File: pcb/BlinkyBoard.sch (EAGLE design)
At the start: 26 parts, among them Q1 16 MHz

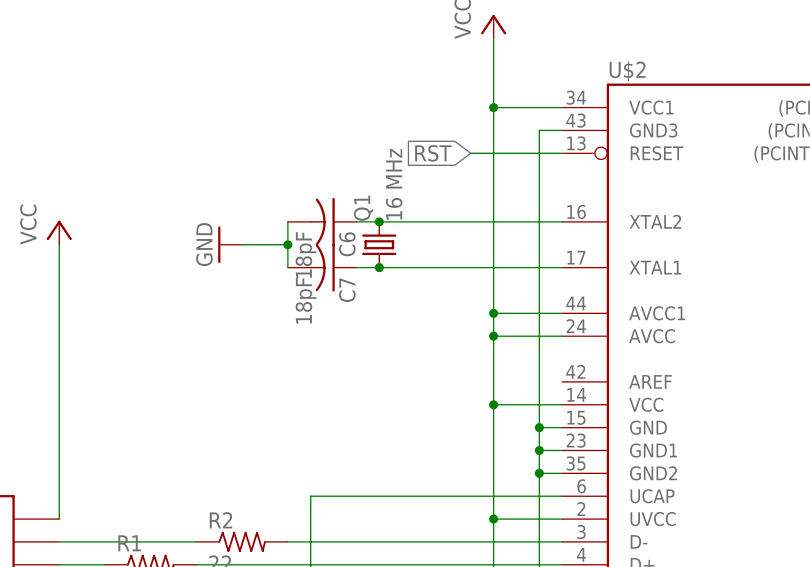
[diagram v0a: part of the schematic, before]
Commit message: Almost have D7 squeezed in, clean up silk
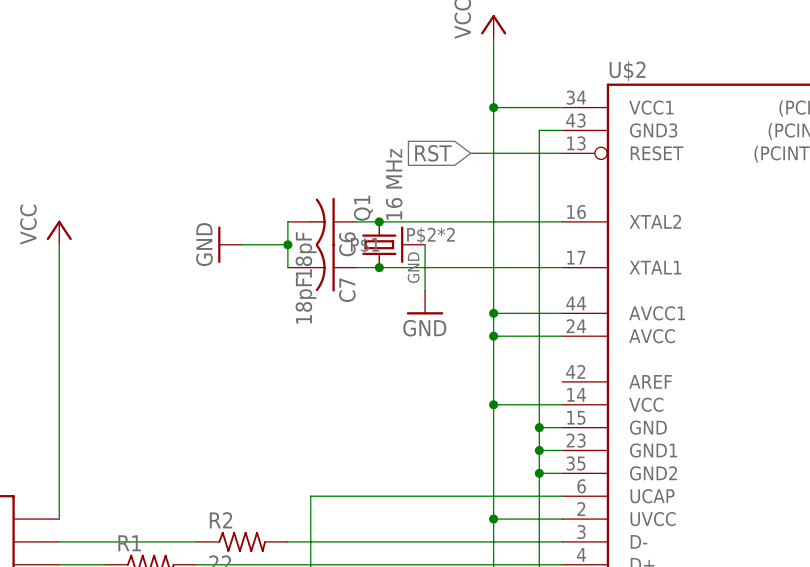
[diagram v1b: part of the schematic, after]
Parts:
- Q1: device blinkiverse:CRYSTAL2520 -> blinkiverse:CRYSTAL_4PAD2520
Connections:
- net GND: now also Q1.P$1
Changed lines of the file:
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@@
 <part name="P+7" library="supply1" deviceset="VCC" device=""/>
 <part name="S1" library="blinkyboard" deviceset="GLOWBOARD_KMR211G" device="" value="Normally open"/>
-<part name="Q1" library="blinkiverse" deviceset="CRYSTAL" device="2520" value="16 MHz"/>
+<part name="Q1" library="blinkiverse" deviceset="CRYSTAL_4PAD" device="2520" value="16 MHz"/>
 <part name="C4" library="blinkiverse" deviceset="C_US" device="" value="0.1uF"/>
 <part name="WS1" library="blinkiverse" deviceset="WS2811_CONNECTOR" device=""/>
@@
 <part name="U$13" library="blinkiverse" deviceset="TEST_PAD_SMT" device=""/>
 <part name="U$14" library="blinkiverse" deviceset="TEST_PAD_SMT" device=""/>
+<part name="GND9" library="supply1" deviceset="GND" device=""/>
 </parts>
 <sheets>
@@
 <instance part="U$13" gate="G$1" x="187.96" y="86.36"/>
 <instance part="U$14" gate="G$1" x="187.96" y="93.98"/>
+<instance part="GND9" gate="1" x="20.32" y="63.5"/>
 </instances>
 <busses>
@@
 <pinref part="U$13" gate="G$1" pin="P$1"/>
 </segment>
+<segment>
+<pinref part="Q1" gate="G$1" pin="P$1"/>
+<pinref part="GND9" gate="1" pin="GND"/>
+<wire x1="20.32" y1="71.12" x2="20.32" y2="66.04" width="0.1524" layer="91"/>
+</segment>
 </net>

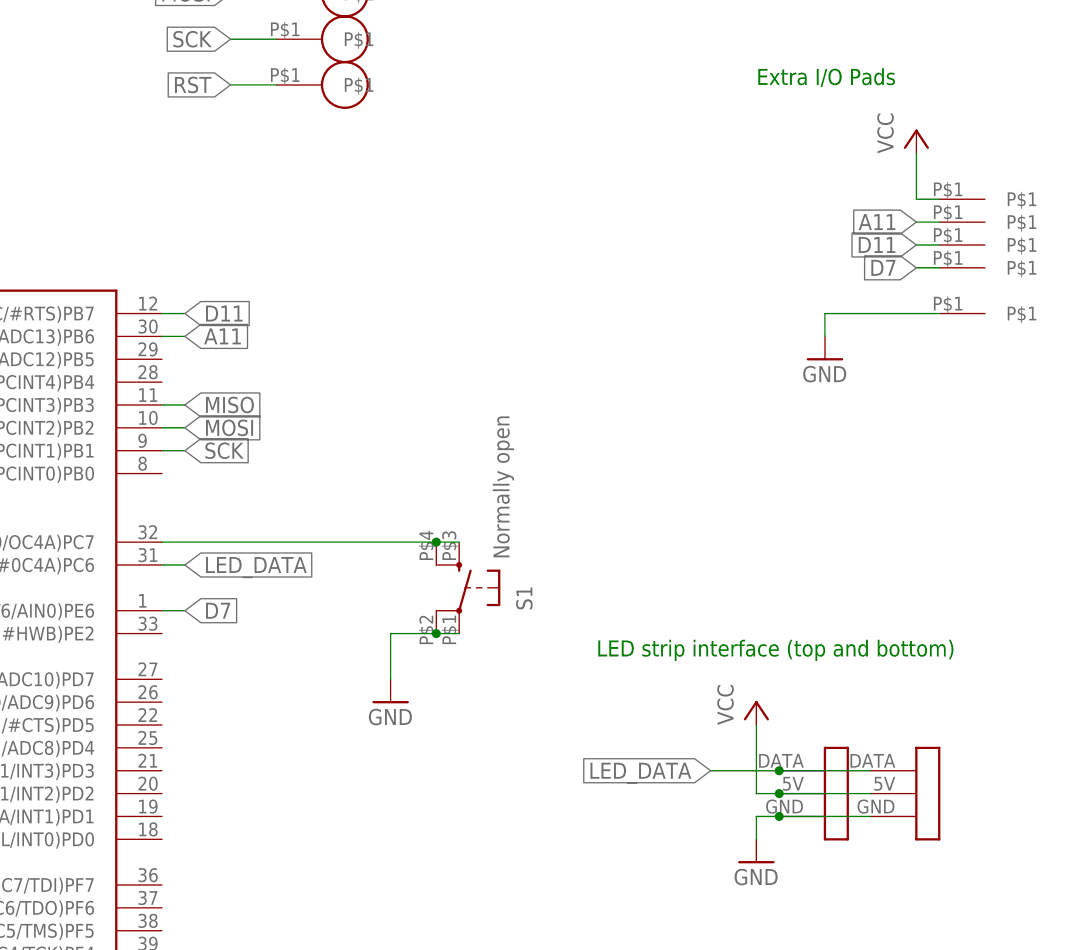
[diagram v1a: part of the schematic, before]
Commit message: RevD candidate- Move switch to D10 (for interrupt capability), then move analog input to A10 and LED_DATA to D13.
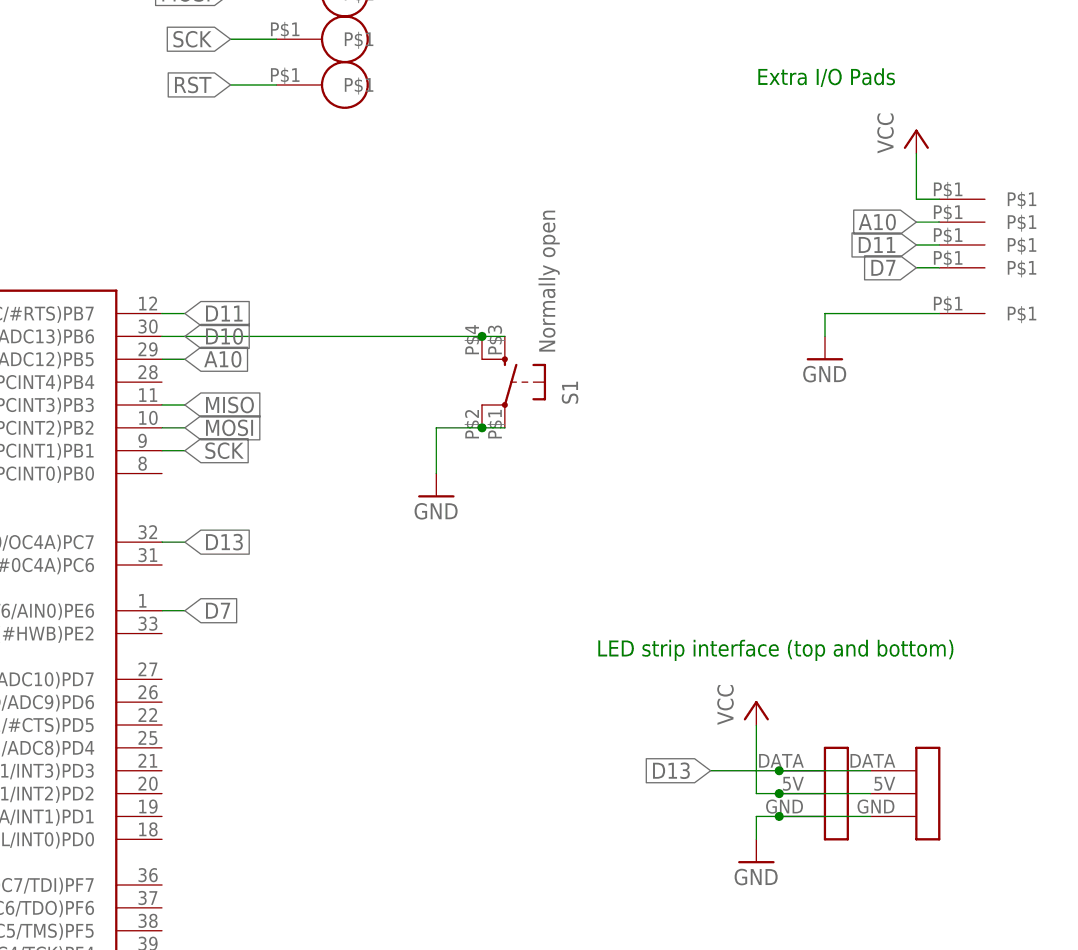
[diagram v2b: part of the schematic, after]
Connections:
- removed net A11: U$11.P$1, U$2.(PCINT6/OC1B/OC4B/ADC13)PB6
- removed net LED_DATA: U$2.(OC3A/#0C4A)PC6, WS1.DATA, WS3.DATA
- removed net N$10: S1.S, S1.S1, U$2.(ICP3/CLK0/OC4A)PC7
- new net A10: U$11.P$1, U$2.(PCINT5/OC1A/#OC4B/ADC12)PB5
- new net D10: S1.S, S1.S1, U$2.(PCINT6/OC1B/OC4B/ADC13)PB6
- new net D13: U$2.(ICP3/CLK0/OC4A)PC7, WS1.DATA, WS3.DATA
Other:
- moved on the sheet: S1
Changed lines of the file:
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@@
 <instance part="C3" gate="G$1" x="-30.48" y="121.92"/>
 <instance part="GND12" gate="1" x="-30.48" y="109.22" rot="MR0"/>
-<instance part="GND7" gate="1" x="121.92" y="43.18"/>
+<instance part="GND7" gate="1" x="127" y="66.04"/>
 <instance part="C6" gate="G$1" x="10.16" y="73.66" rot="R270"/>
 <instance part="C7" gate="G$1" x="10.16" y="68.58" rot="R270"/>
@@
 <instance part="P+6" gate="VCC" x="27.94" y="96.52"/>
 <instance part="P+7" gate="VCC" x="-30.48" y="132.08"/>
-<instance part="S1" gate="1" x="129.54" y="55.88" rot="MR0"/>
+<instance part="S1" gate="1" x="134.62" y="78.74" rot="MR0"/>
 <instance part="Q1" gate="G$1" x="15.24" y="71.12" rot="R90"/>
 <instance part="C4" gate="G$1" x="-20.32" y="121.92"/>
@@
 </segment>
 <segment>
-<wire x1="121.92" y1="45.72" x2="121.92" y2="50.8" width="0.1524" layer="91"/>
+<wire x1="127" y1="68.58" x2="127" y2="73.66" width="0.1524" layer="91"/>
 <pinref part="GND7" gate="1" pin="GND"/>
 <pinref part="S1" gate="1" pin="P"/>
 <pinref part="S1" gate="1" pin="P1"/>
-<wire x1="129.54" y1="50.8" x2="127" y2="50.8" width="0.1524" layer="91"/>
-<wire x1="127" y1="50.8" x2="121.92" y2="50.8" width="0.1524" layer="91"/>
-<junction x="127" y="50.8"/>
+<wire x1="134.62" y1="73.66" x2="132.08" y2="73.66" width="0.1524" layer="91"/>
+<wire x1="132.08" y1="73.66" x2="127" y2="73.66" width="0.1524" layer="91"/>
+<junction x="132.08" y="73.66"/>
 </segment>
 <segment>
@@
 </segment>
 </net>
-<net name="N$10" class="0">
-<segment>
-<pinref part="U$2" gate="G$1" pin="(ICP3/CLK0/OC4A)PC7"/>
+<net name="D10" class="0">
+<segment>
 <pinref part="S1" gate="1" pin="S1"/>
-<wire x1="96.52" y1="60.96" x2="127" y2="60.96" width="0.1524" layer="91"/>
 <pinref part="S1" gate="1" pin="S"/>
-<wire x1="129.54" y1="60.96" x2="127" y2="60.96" width="0.1524" layer="91"/>
-<junction x="127" y="60.96"/>
+<wire x1="134.62" y1="83.82" x2="132.08" y2="83.82" width="0.1524" layer="91"/>
+<pinref part="U$2" gate="G$1" pin="(PCINT6/OC1B/OC4B/ADC13)PB6"/>
+<wire x1="96.52" y1="83.82" x2="132.08" y2="83.82" width="0.1524" layer="91"/>
+<junction x="132.08" y="83.82"/>
+<label x="99.06" y="83.82" size="1.778" layer="95" xref="yes"/>
 </segment>
 </net>
@@
 </segment>
 </net>
-<net name="A11" class="0">
-<segment>
-<pinref part="U$2" gate="G$1" pin="(PCINT6/OC1B/OC4B/ADC13)PB6"/>
-<wire x1="96.52" y1="83.82" x2="99.06" y2="83.82" width="0.1524" layer="91"/>
-<label x="99.06" y="83.82" size="1.778" layer="95" xref="yes"/>
-</segment>
-<segment>
-<label x="180.34" y="96.52" size="1.778" layer="95" rot="R180" xref="yes"/>
-<wire x1="182.88" y1="96.52" x2="180.34" y2="96.52" width="0.1524" layer="91"/>
-<pinref part="U$11" gate="G$1" pin="P$1"/>
-</segment>
-</net>
-<net name="LED_DATA" class="0">
-<segment>
-<pinref part="U$2" gate="G$1" pin="(OC3A/#0C4A)PC6"/>
-<wire x1="96.52" y1="58.42" x2="99.06" y2="58.42" width="0.1524" layer="91"/>
-<label x="99.06" y="58.42" size="1.778" layer="95" xref="yes"/>
-</segment>
+<net name="D13" class="0">
 <segment>
 <pinref part="WS1" gate="G$1" pin="DATA"/>
@@
 <wire x1="175.26" y1="35.56" x2="165.1" y2="35.56" width="0.1524" layer="91"/>
 <junction x="165.1" y="35.56"/>
+</segment>
+<segment>
+<pinref part="U$2" gate="G$1" pin="(ICP3/CLK0/OC4A)PC7"/>
+<wire x1="96.52" y1="60.96" x2="99.06" y2="60.96" width="0.1524" layer="91"/>
+<label x="99.06" y="60.96" size="1.778" layer="95" xref="yes"/>
 </segment>
 </net>
@@
 </segment>
 </net>
+<net name="A10" class="0">
+<segment>
+<pinref part="U$2" gate="G$1" pin="(PCINT5/OC1A/#OC4B/ADC12)PB5"/>
+<wire x1="96.52" y1="81.28" x2="99.06" y2="81.28" width="0.1524" layer="91"/>
+<label x="99.06" y="81.28" size="1.778" layer="95" xref="yes"/>
+</segment>
+<segment>
+<label x="180.34" y="96.52" size="1.778" layer="95" rot="R180" xref="yes"/>
+<wire x1="182.88" y1="96.52" x2="180.34" y2="96.52" width="0.1524" layer="91"/>
+<pinref part="U$11" gate="G$1" pin="P$1"/>
+</segment>
+</net>

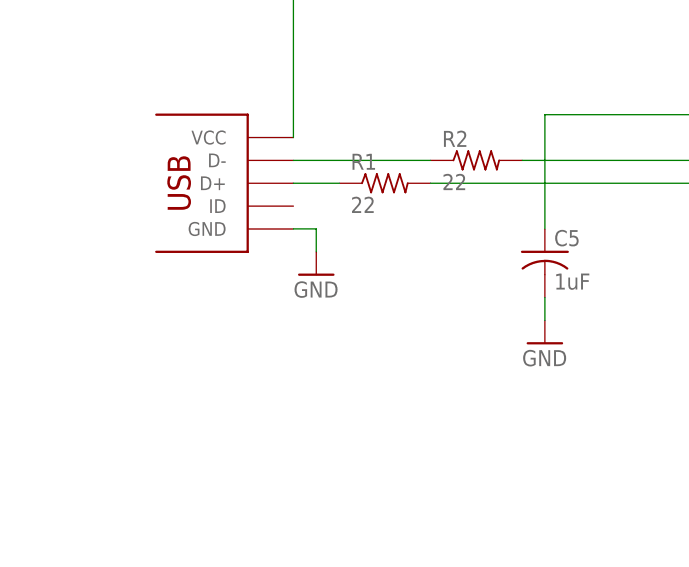
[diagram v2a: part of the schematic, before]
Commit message: Fix copper planes under usb connector
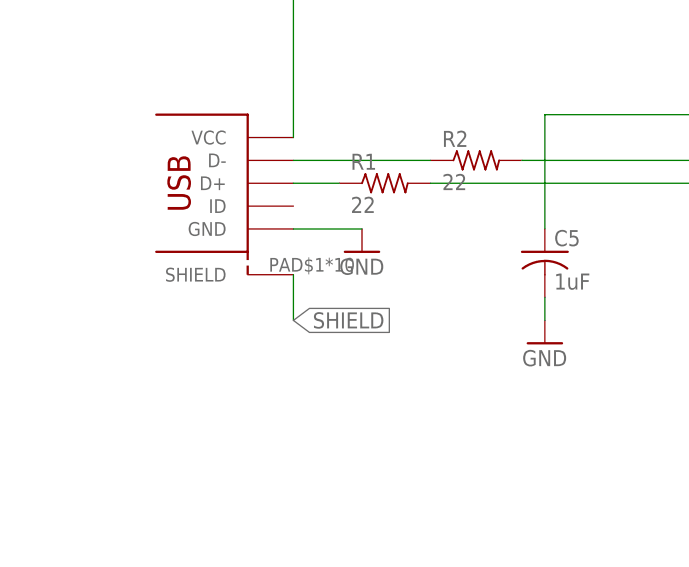
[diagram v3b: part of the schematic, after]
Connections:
- new net SHIELD: U$4.SHIELD
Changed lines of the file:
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@@
 <instance part="P+4" gate="VCC" x="-20.32" y="73.66"/>
 <instance part="U$4" gate="G$1" x="-27.94" y="35.56"/>
-<instance part="GND5" gate="1" x="-17.78" y="25.4"/>
+<instance part="GND5" gate="1" x="-12.7" y="27.94"/>
 <instance part="U$1" gate="G$1" x="114.3" y="127"/>
 <instance part="U$3" gate="G$1" x="114.3" y="121.92"/>
@@
 <segment>
 <pinref part="U$4" gate="G$1" pin="GND"/>
-<wire x1="-20.32" y1="30.48" x2="-17.78" y2="30.48" width="0.1524" layer="91"/>
+<wire x1="-20.32" y1="30.48" x2="-12.7" y2="30.48" width="0.1524" layer="91"/>
 <pinref part="GND5" gate="1" pin="GND"/>
-<wire x1="-17.78" y1="30.48" x2="-17.78" y2="27.94" width="0.1524" layer="91"/>
 </segment>
 <segment>
@@
 </segment>
 </net>
+<net name="SHIELD" class="0">
+<segment>
+<pinref part="U$4" gate="G$1" pin="SHIELD"/>
+<wire x1="-20.32" y1="25.4" x2="-20.32" y2="20.32" width="0.1524" layer="91"/>
+<label x="-20.32" y="20.32" size="1.778" layer="95" xref="yes"/>
+</segment>
+</net>

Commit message: Reorganize test designs, add test card, fix silk on main PCBA
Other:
- note added: "BlinkyTape LED controller RevD"
- note added: "http://blinkiverse.com"
- note removed: "BlinkyBoard LED controller RevB"
- note removed: "http://blinkyverse.com"
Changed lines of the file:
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@@
 <sheet>
 <plain>
-<text x="104.14" y="-30.48" size="2.54" layer="94">BlinkyBoard LED controller RevB</text>
-<text x="104.14" y="-35.56" size="2.54" layer="94">http://blinkyverse.com</text>
+<text x="104.14" y="-30.48" size="2.54" layer="94">BlinkyTape LED controller RevD</text>
+<text x="104.14" y="-35.56" size="2.54" layer="94">http://blinkiverse.com</text>
 <text x="177.8" y="-30.48" size="2.54" layer="94">CC 2.5 BY-SA</text>
 <text x="190.5" y="-53.34" size="2.54" layer="94">1</text>

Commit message: PCB design fix: add cream to all USB ground pads!
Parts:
- WS1, WS3: value WS2811_CONNECTOR -> WS2811_CONNECTORSTRIP; device blinkiverse:WS2811_CONNECTOR -> blinkiverse:WS2811_CONNECTORSTRIP
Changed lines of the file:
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@@
 <part name="Q1" library="blinkiverse" deviceset="CRYSTAL_4PAD" device="2520" value="16 MHz"/>
 <part name="C4" library="blinkiverse" deviceset="C_US" device="" value="0.1uF"/>
-<part name="WS1" library="blinkiverse" deviceset="WS2811_CONNECTOR" device=""/>
+<part name="WS1" library="blinkiverse" deviceset="WS2811_CONNECTOR" device="STRIP"/>
 <part name="P+3" library="supply1" deviceset="VCC" device=""/>
 <part name="GND4" library="supply1" deviceset="GND" device=""/>
@@
 <part name="GND1" library="supply1" deviceset="GND" device=""/>
 <part name="GND2" library="supply1" deviceset="GND" device=""/>
-<part name="WS3" library="blinkiverse" deviceset="WS2811_CONNECTOR" device=""/>
+<part name="WS3" library="blinkiverse" deviceset="WS2811_CONNECTOR" device="STRIP"/>
 <part name="P+5" library="supply1" deviceset="VCC" device=""/>
 <part name="U$10" library="blinkiverse" deviceset="TEST_PAD_SMT" device=""/>

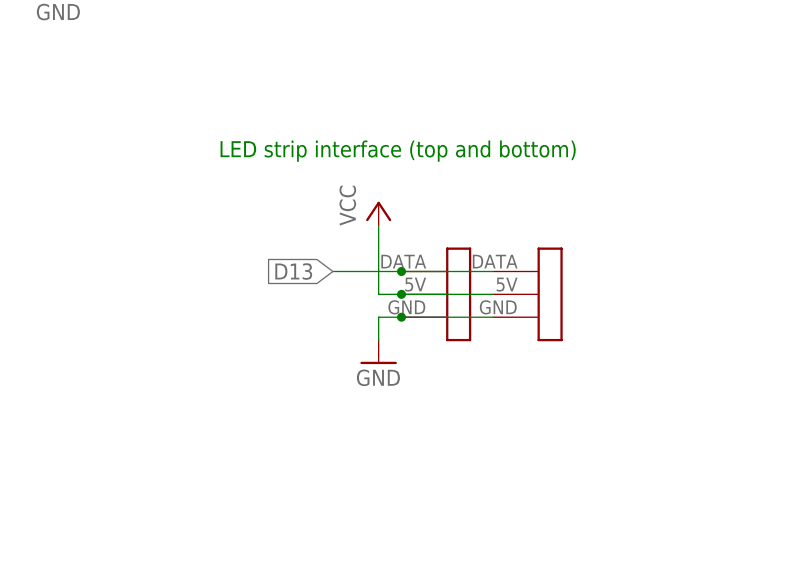
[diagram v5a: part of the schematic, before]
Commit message: RevF release: modify pads to support WS2811B
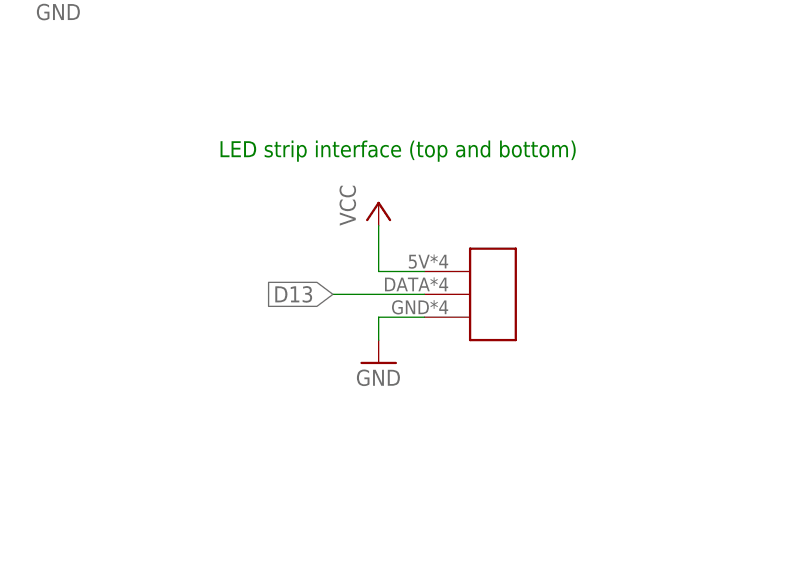
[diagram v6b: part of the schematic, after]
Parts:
- removed WS1, WS3: WS2811_CONNECTORSTRIP, blinkiverse:WS2811_CONNECTORSTRIP
- added U$9: WS2812B_CONNECTOR, blinkiverse:WS2812B_CONNECTOR
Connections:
- net D13: now also U$9.DATA; no longer WS1.DATA, WS3.DATA
- net GND: now also U$9.GND; no longer WS1.GND, WS3.GND
- net VCC: now also U$9.5V; no longer WS1.5V, WS3.5V
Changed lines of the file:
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@@
 <part name="Q1" library="blinkiverse" deviceset="CRYSTAL_4PAD" device="2520" value="16 MHz"/>
 <part name="C4" library="blinkiverse" deviceset="C_US" device="" value="0.1uF"/>
-<part name="WS1" library="blinkiverse" deviceset="WS2811_CONNECTOR" device="STRIP"/>
 <part name="P+3" library="supply1" deviceset="VCC" device=""/>
 <part name="GND4" library="supply1" deviceset="GND" device=""/>
@@
 <part name="GND1" library="supply1" deviceset="GND" device=""/>
 <part name="GND2" library="supply1" deviceset="GND" device=""/>
-<part name="WS3" library="blinkiverse" deviceset="WS2811_CONNECTOR" device="STRIP"/>
 <part name="P+5" library="supply1" deviceset="VCC" device=""/>
 <part name="U$10" library="blinkiverse" deviceset="TEST_PAD_SMT" device=""/>
@@
 <part name="U$14" library="blinkiverse" deviceset="TEST_PAD_SMT" device=""/>
 <part name="GND9" library="supply1" deviceset="GND" device=""/>
+<part name="U$9" library="blinkiverse" deviceset="WS2812B_CONNECTOR" device=""/>
 </parts>
 <sheets>
@@
 <instance part="Q1" gate="G$1" x="15.24" y="71.12" rot="R90"/>
 <instance part="C4" gate="G$1" x="-20.32" y="121.92"/>
-<instance part="WS1" gate="G$1" x="172.72" y="33.02"/>
 <instance part="P+3" gate="VCC" x="162.56" y="43.18"/>
 <instance part="GND4" gate="1" x="162.56" y="25.4"/>
@@
 <instance part="GND1" gate="1" x="101.6" y="132.08" rot="R270"/>
 <instance part="GND2" gate="1" x="170.18" y="81.28"/>
-<instance part="WS3" gate="G$1" x="182.88" y="33.02"/>
 <instance part="P+5" gate="VCC" x="180.34" y="106.68"/>
 <instance part="U$10" gate="G$1" x="187.96" y="91.44"/>
@@
 <instance part="U$14" gate="G$1" x="187.96" y="93.98"/>
 <instance part="GND9" gate="1" x="20.32" y="63.5"/>
+<instance part="U$9" gate="G$1" x="172.72" y="33.02"/>
 </instances>
 <busses>
@@
 </segment>
 <segment>
-<pinref part="WS1" gate="G$1" pin="GND"/>
-<wire x1="165.1" y1="30.48" x2="162.56" y2="30.48" width="0.1524" layer="91"/>
 <pinref part="GND4" gate="1" pin="GND"/>
 <wire x1="162.56" y1="30.48" x2="162.56" y2="27.94" width="0.1524" layer="91"/>
-<pinref part="WS3" gate="G$1" pin="GND"/>
-<wire x1="175.26" y1="30.48" x2="165.1" y2="30.48" width="0.1524" layer="91"/>
-<junction x="165.1" y="30.48"/>
+<pinref part="U$9" gate="G$1" pin="GND"/>
+<wire x1="162.56" y1="30.48" x2="167.64" y2="30.48" width="0.1524" layer="91"/>
 </segment>
 <segment>
@@
 <net name="D13" class="0">
 <segment>
-<pinref part="WS1" gate="G$1" pin="DATA"/>
-<wire x1="165.1" y1="35.56" x2="157.48" y2="35.56" width="0.1524" layer="91"/>
-<label x="157.48" y="35.56" size="1.778" layer="95" rot="R180" xref="yes"/>
-<pinref part="WS3" gate="G$1" pin="DATA"/>
-<wire x1="175.26" y1="35.56" x2="165.1" y2="35.56" width="0.1524" layer="91"/>
-<junction x="165.1" y="35.56"/>
-</segment>
-<segment>
 <pinref part="U$2" gate="G$1" pin="(ICP3/CLK0/OC4A)PC7"/>
 <wire x1="96.52" y1="60.96" x2="99.06" y2="60.96" width="0.1524" layer="91"/>
 <label x="99.06" y="60.96" size="1.778" layer="95" xref="yes"/>
+</segment>
+<segment>
+<wire x1="167.64" y1="33.02" x2="157.48" y2="33.02" width="0.1524" layer="91"/>
+<label x="157.48" y="33.02" size="1.778" layer="95" rot="R180" xref="yes"/>
+<pinref part="U$9" gate="G$1" pin="DATA"/>
 </segment>
 </net>
@@
 </segment>
 <segment>
-<pinref part="WS1" gate="G$1" pin="5V"/>
-<wire x1="165.1" y1="33.02" x2="162.56" y2="33.02" width="0.1524" layer="91"/>
 <pinref part="P+3" gate="VCC" pin="VCC"/>
-<wire x1="162.56" y1="33.02" x2="162.56" y2="40.64" width="0.1524" layer="91"/>
-<pinref part="WS3" gate="G$1" pin="5V"/>
-<wire x1="165.1" y1="33.02" x2="175.26" y2="33.02" width="0.1524" layer="91"/>
-<junction x="165.1" y="33.02"/>
+<wire x1="162.56" y1="35.56" x2="162.56" y2="40.64" width="0.1524" layer="91"/>
+<pinref part="U$9" gate="G$1" pin="5V"/>
+<wire x1="162.56" y1="35.56" x2="167.64" y2="35.56" width="0.1524" layer="91"/>
 </segment>
 <segment>
@@
 </sheet>
 </sheets>
+<errors>
+</errors>
 </schematic>
 </drawing>
